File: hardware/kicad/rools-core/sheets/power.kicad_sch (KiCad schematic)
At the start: 22 parts, among them U1 TPS54302, U2 AP2112K-3.3

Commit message: Wire rools-core KiCad sheets with global labels and UI peripherals.
Migrate inter-sheet nets to global labels and flesh out UI, power, and
child-sheet power entry so net names align with pins.h for PCB routing.

Co-authored-by: Cursor <cursoragent@cursor.com>
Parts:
- R1: value 10K -> 73.2k
- R2: value 2K -> 10k
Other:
- note added: "U1 FB: R1=73.2k R2=10k → 5.0V (Vref=596mV); EN R3/R4=330k/100k"
- note removed: "C/L/R_FB 值为骨架占位, 按 TPS54302 手册核算"
- moved on the sheet: C1, C2, C3, C4, C5, C6, D1, D2, FB1, FB2, L1, P1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

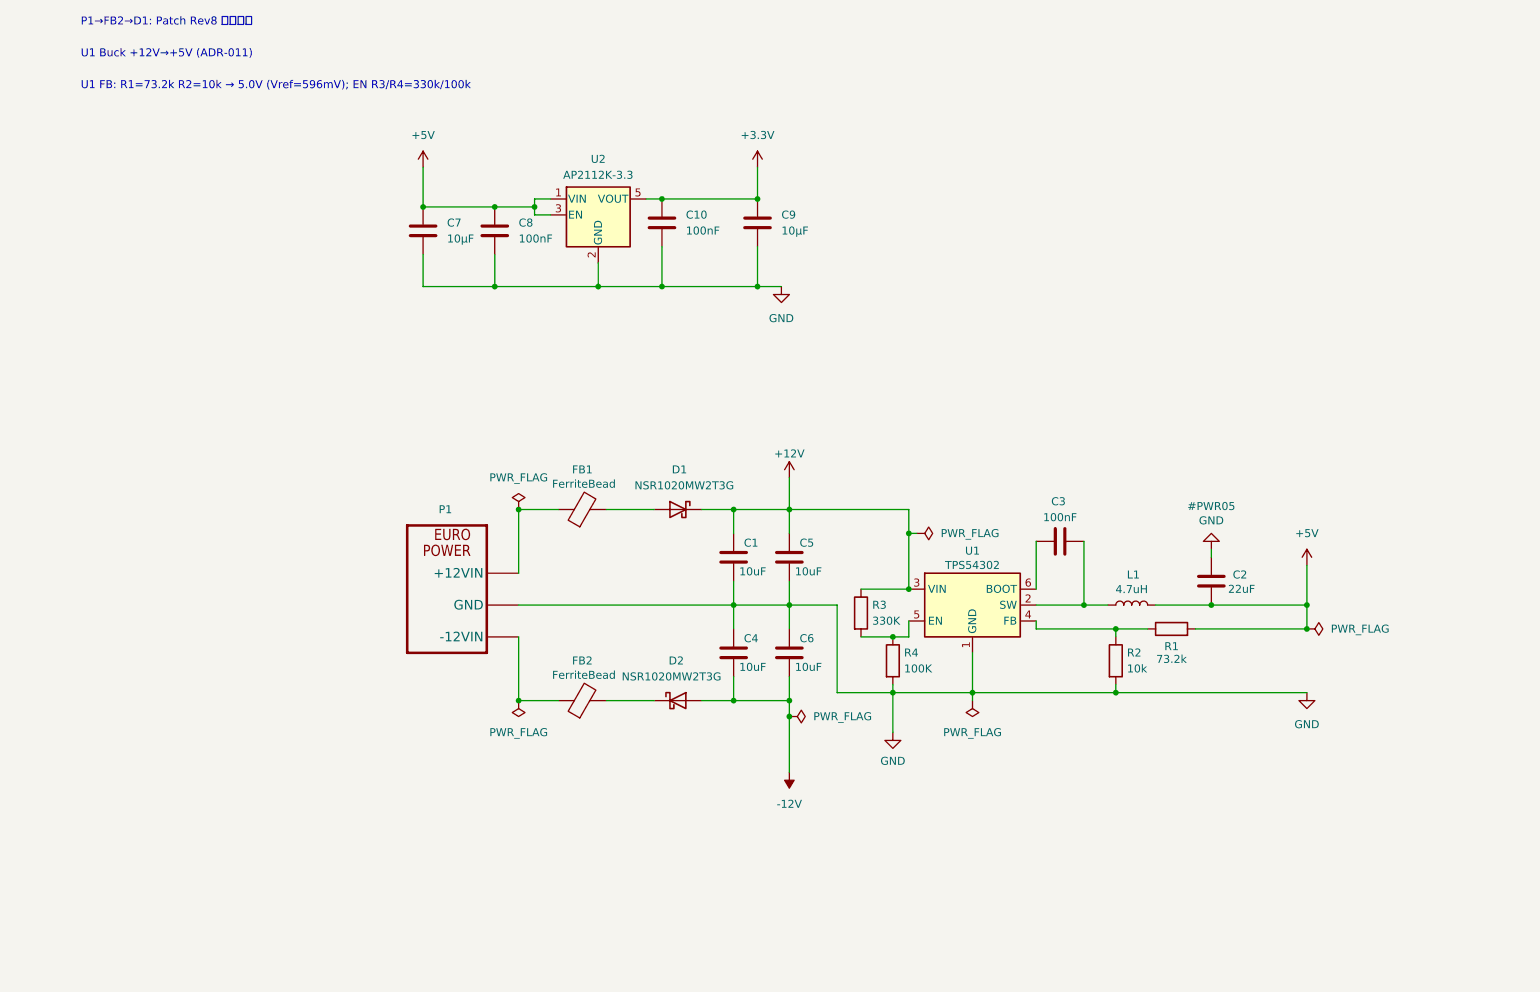
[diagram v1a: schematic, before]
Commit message: Add QSPI settings persistence, CV calibration app, and CV output driver.
Co-authored-by: Cursor <cursoragent@cursor.com>
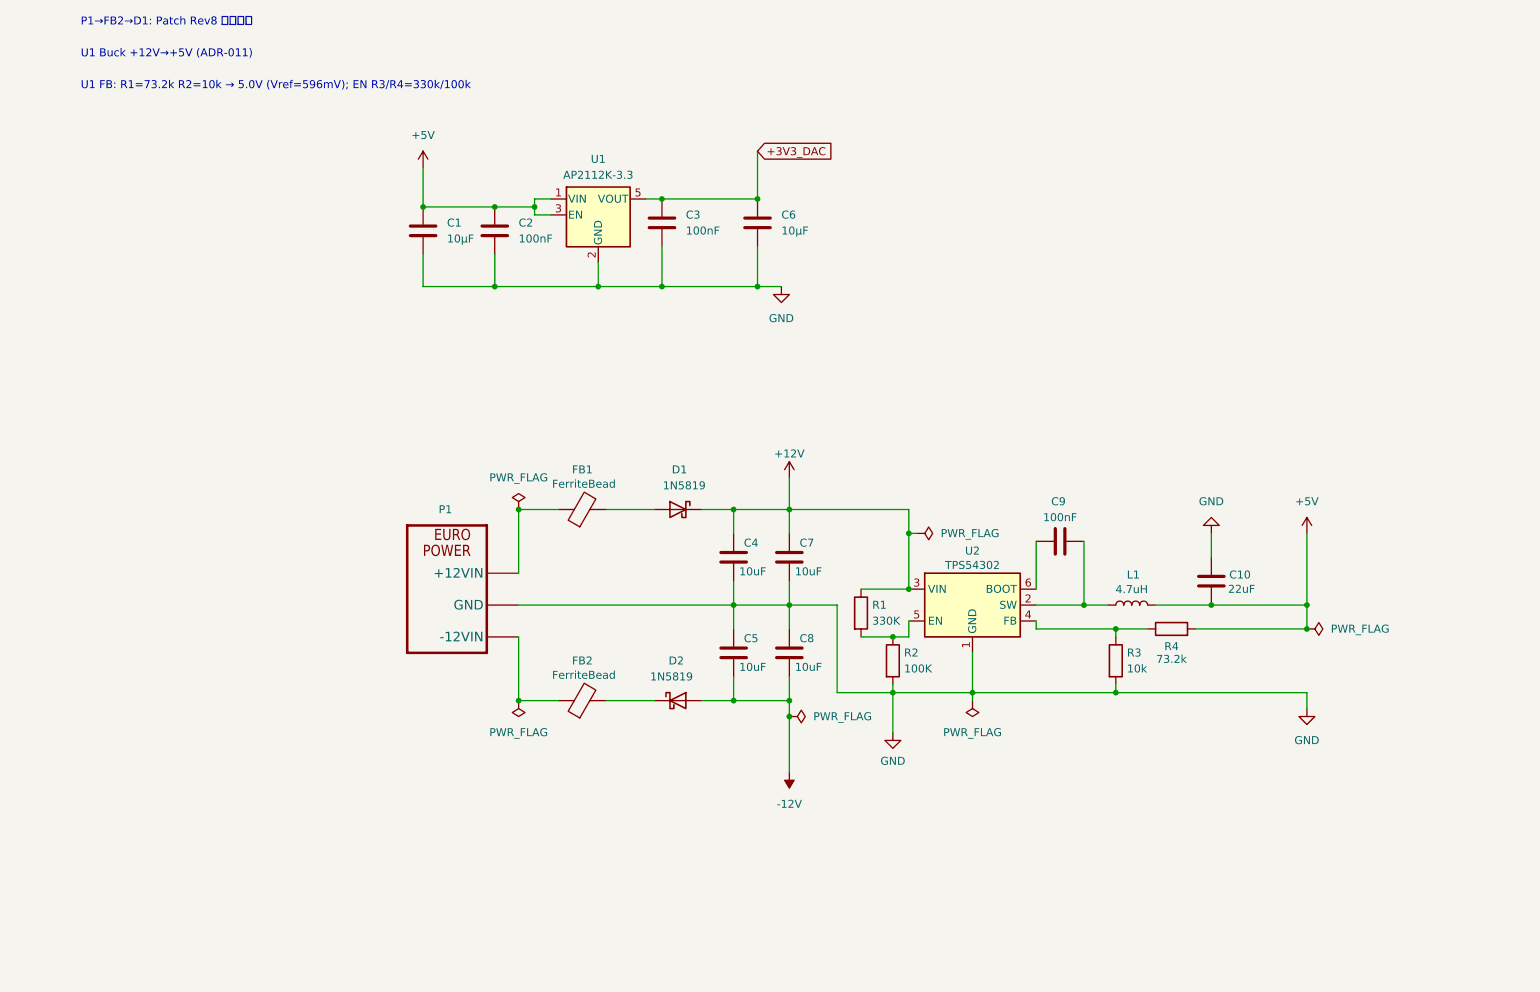
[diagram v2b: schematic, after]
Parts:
- D1, D2: value NSR1020MW2T3G -> 1N5819; footprint (none) -> Diode_THT:D_DO-41_SOD81_P10.16mm_Horizontal; symbol Device:D_Schottky -> Diode:1N5819
- renumbered C7 to C1, C2 to C10, C8 to C2, C10 to C3, C1 to C4, C4 to C5, C9 to C6, C5 to C7, C6 to C8, C3 to C9, R3 to R1, R4 to R2, R2 to R3, R1 to R4, U2 to U1, U1 to U2
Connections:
- net +3.3V renamed +3V3_DAC

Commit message: Sync Core schematic Rev 0.2 with docs and firmware.
Align DAC8565/OPA4171 CV path (2.5V internal ref, 12.5k/100k), LM393 power-fail hold-up, and SPI1 CV driver fixes (LDAC polarity, debounced save with backlight off).

Co-authored-by: Cursor <cursoragent@cursor.com>
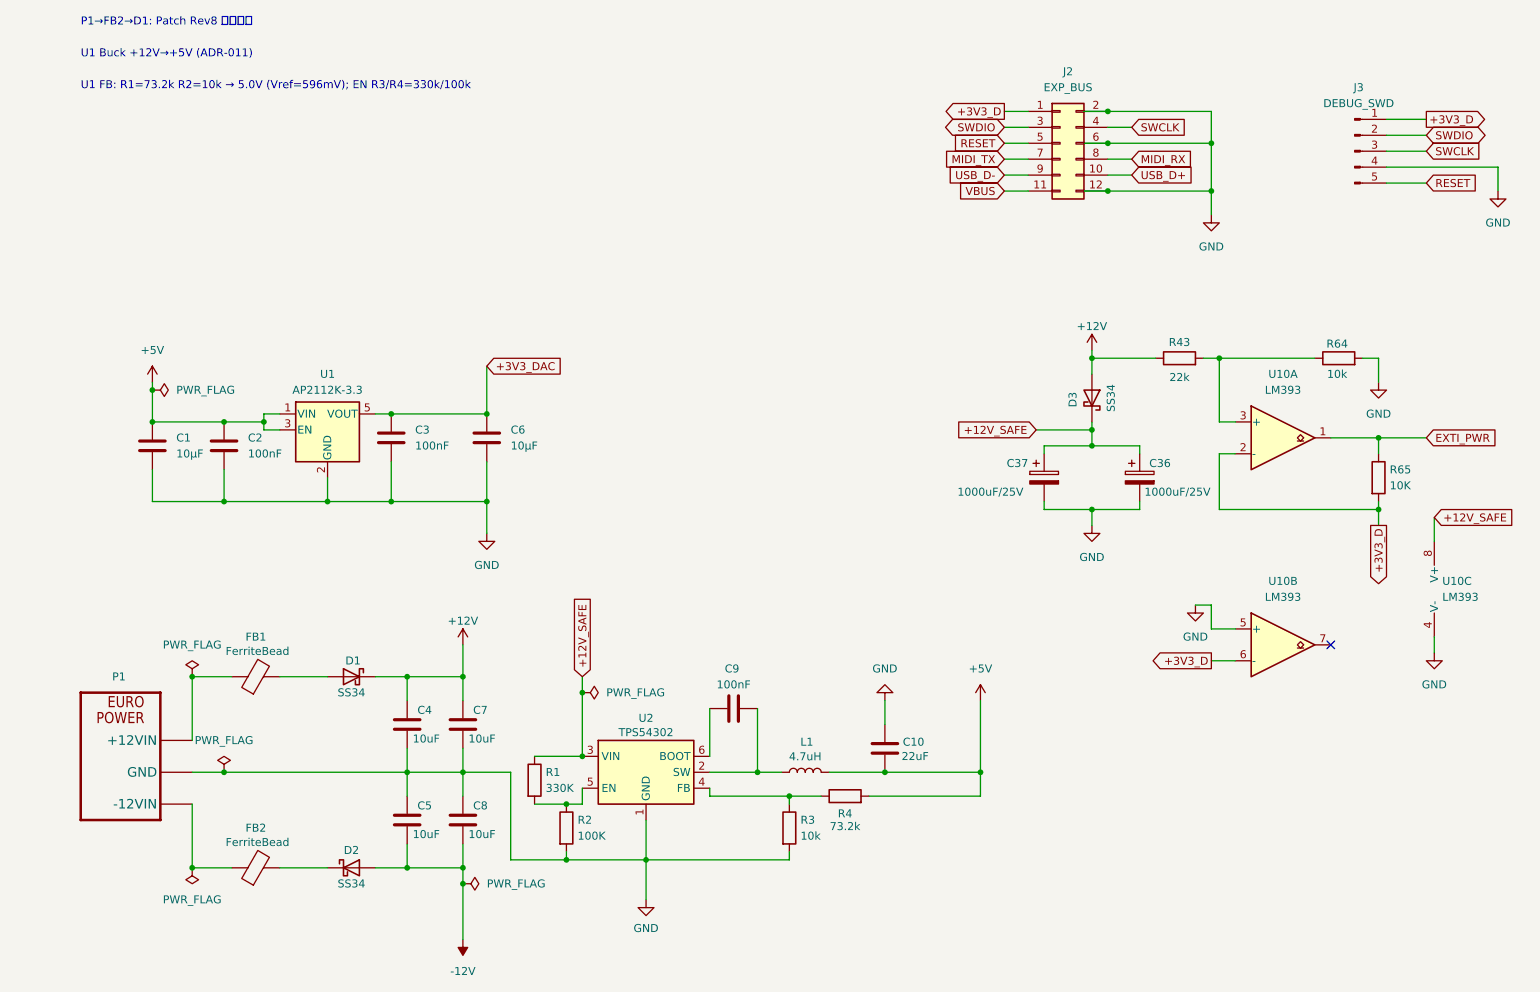
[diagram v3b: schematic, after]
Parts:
- added C36, C37: 1000uF/25V, symbol Device:C_Polarized
- added D3: SS34, Diode_SMD:D_SMA, symbol Diode:SS34
- added J2: EXP_BUS, symbol Connector_Generic:Conn_02x06_Odd_Even
- added J3: DEBUG_SWD, symbol Connector:Conn_01x05_Pin
- added R43: 22k, symbol Device:R
- added R64: 10k, symbol Device:R
- added R65: 10K, symbol Device:R
- added U10: LM393, symbol Comparator:LM393
- D1, D2: value 1N5819 -> SS34; footprint Diode_THT:D_DO-41_SOD81_P10.16mm_Horizontal -> Diode_SMD:D_SMA; symbol Diode:1N5819 -> Diode:SS34
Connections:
- net +12V: now also D3.2 (A), R43.1; no longer R1.1, U2.3 (VIN)
- net GND: now also C36.2, C37.2, J2.12 (Pin_12), J2.2 (Pin_2), J2.6 (Pin_6), J3.4 (Pin_4), R64.2, U10.4 (V-), U10.5 (+)
- new net: R43.2, R64.1, U10.3 (+)
- new net +12V_SAFE: C36.1, C37.1, D3.1 (K), R1.1, U10.8 (V+), U2.3 (VIN)
- new net +3V3_D: J2.1 (Pin_1), J3.1 (Pin_1), R65.2, U10.2 (-), U10.6 (-)
- new net EXTI_PWR: R65.1, U10.1
- new net MIDI_RX: J2.8 (Pin_8)
- new net MIDI_TX: J2.7 (Pin_7)
- new net RESET: J2.5 (Pin_5), J3.5 (Pin_5)
- new net SWCLK: J2.4 (Pin_4), J3.3 (Pin_3)
- new net SWDIO: J2.3 (Pin_3), J3.2 (Pin_2)
- new net USB_D+: J2.10 (Pin_10)
- new net USB_D-: J2.9 (Pin_9)
- new net VBUS: J2.11 (Pin_11)
- no-connect marks 0 -> 1
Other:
- moved on the sheet: C1, C10, C2, C3, C4, C5, C6, C7, C8, C9, D1, D2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

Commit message: Finalize Core schematic pin map and JLC BOM for assembly.
MIDI USART1 on D13/D14, DAC8565 on D26/D27, and document P2 EXP_BUS so Exp I/O no longer conflicts with CV Out.

Co-authored-by: Cursor <cursoragent@cursor.com>
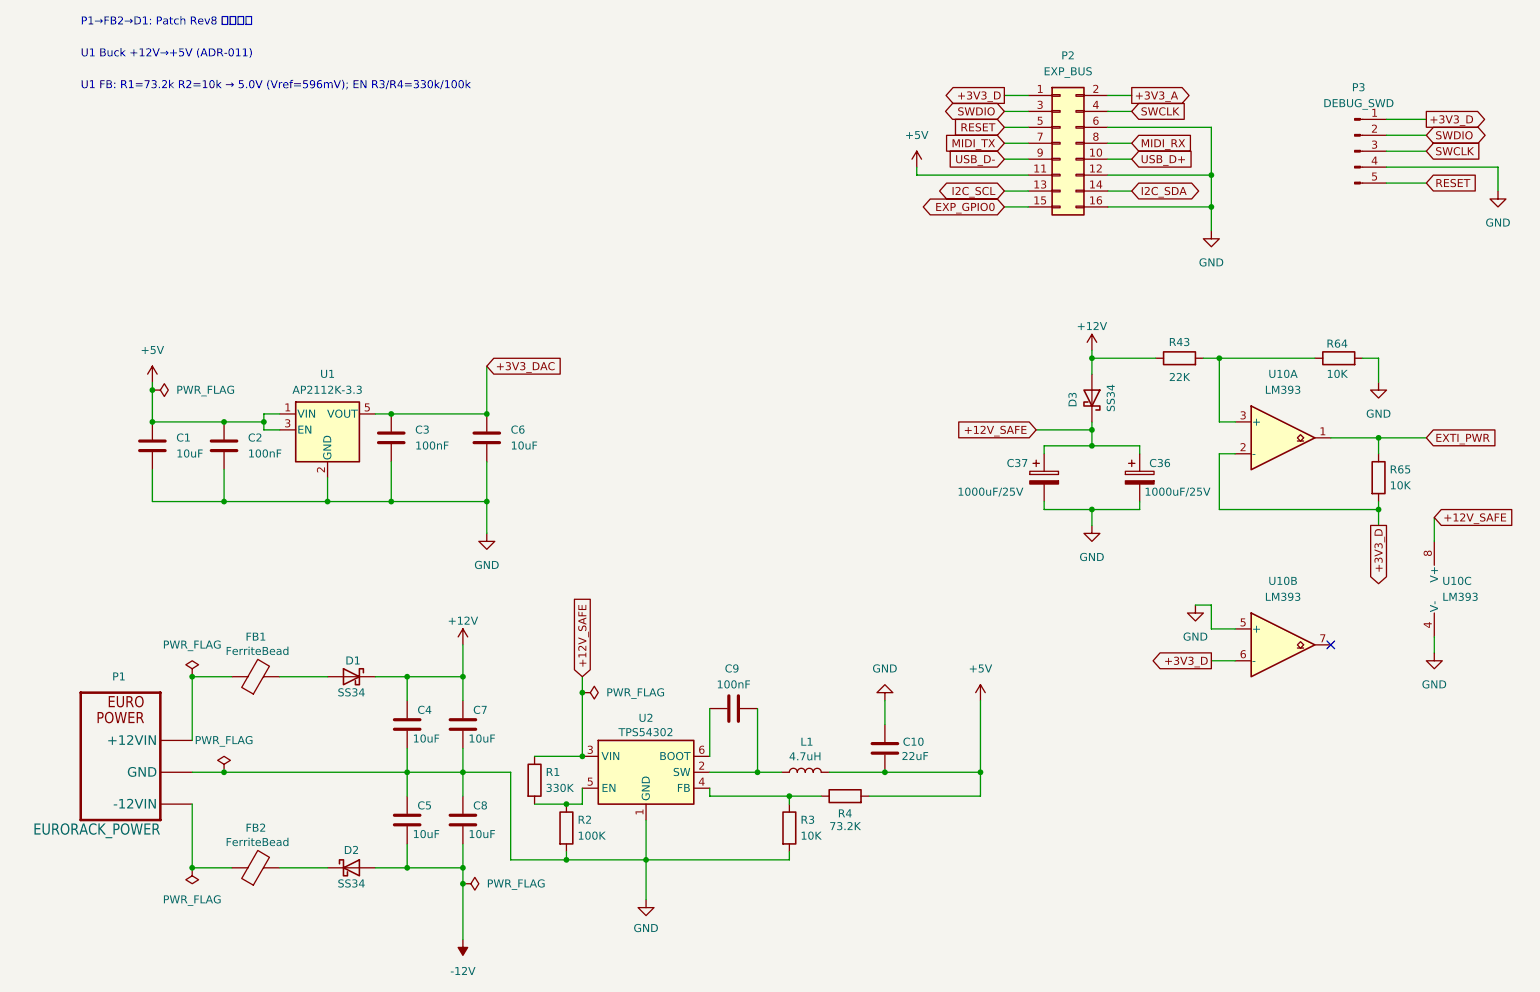
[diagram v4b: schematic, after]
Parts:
- C1, C6: value 10µF -> 10uF; footprint (none) -> Capacitor_SMD:C_0603_1608Metric; LCSC (none) -> C96446
- C10: footprint (none) -> Capacitor_SMD:C_0805_2012Metric; LCSC (none) -> C45783
- C2, C3, C9: footprint (none) -> Capacitor_SMD:C_0603_1608Metric; LCSC (none) -> C14663
- C36, C37: footprint (none) -> Capacitor_SMD:CP_Elec_10x10.5; LCSC (none) -> C49256851
- C4, C5, C7, C8: footprint (none) -> Capacitor_SMD:C_0603_1608Metric; LCSC (none) -> C96446
- D1, D2, D3: LCSC (none) -> C8678
- FB1, FB2: footprint (none) -> Inductor_SMD:L_0603_1608Metric; LCSC (none) -> C1015
- L1: footprint (none) -> Inductor_SMD:L_Taiyo-Yuden_NR-40xx; LCSC (none) -> C167874
- P1: value (none) -> EURORACK_POWER; footprint Connector_PinHeader_1.00mm:PinHeader_2x05_P1.00mm_Horizontal -> Connector_IDC:IDC-Header_2x08_P2.54mm_Vertical; LCSC (none) -> C3406
- P2: renamed from J2; footprint (none) -> Connector_PinHeader_2.54mm:PinHeader_2x08_P2.54mm_Vertical; symbol Connector_Generic:Conn_02x06_Odd_Even -> Connector_Generic:Conn_02x08_Odd_Even
- P3: renamed from J3; footprint (none) -> Connector_PinHeader_2.54mm:PinHeader_1x05_P2.54mm_Vertical
- R1: footprint (none) -> Resistor_SMD:R_0603_1608Metric; LCSC (none) -> C23137
- R2: footprint (none) -> Resistor_SMD:R_0603_1608Metric; LCSC (none) -> C25803
- R3, R64: value 10k -> 10K; footprint (none) -> Resistor_SMD:R_0603_1608Metric; LCSC (none) -> C25804
- R4: value 73.2k -> 73.2K; footprint (none) -> Resistor_SMD:R_0603_1608Metric; LCSC (none) -> C14890
- R43: value 22k -> 22K; footprint (none) -> Resistor_SMD:R_0603_1608Metric; LCSC (none) -> C23162
- R65: footprint (none) -> Resistor_SMD:R_0603_1608Metric; LCSC (none) -> C25804
- U1: LCSC (none) -> C51118
- U10: footprint (none) -> Package_SO:SOIC-8_3.9x4.9mm_P1.27mm; LCSC (none) -> C7955
- U2: footprint (none) -> Package_TO_SOT_SMD:TSOT-23-6; LCSC (none) -> C311903
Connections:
- net VBUS is gone; now on net +5V: P2.11 (Pin_11)
- net GND: now also P2.16 (Pin_16); no longer P2.2 (Pin_2)
- new net +3V3_A: P2.2 (Pin_2)
- new net EXP_GPIO0: P2.15 (Pin_15)
- new net I2C_SCL: P2.13 (Pin_13)
- new net I2C_SDA: P2.14 (Pin_14)
